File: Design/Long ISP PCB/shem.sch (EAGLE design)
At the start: 49 parts, among them IC1 4511N, IC2 4511N, J1 9V_POWER_JACK, Q1 600mA/40V, Q2 600mA/40V, Q3 600mA/40V, Q4 600mA/40V, Q5 600mA/40V, U2 328P, U3 SN74HC595N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

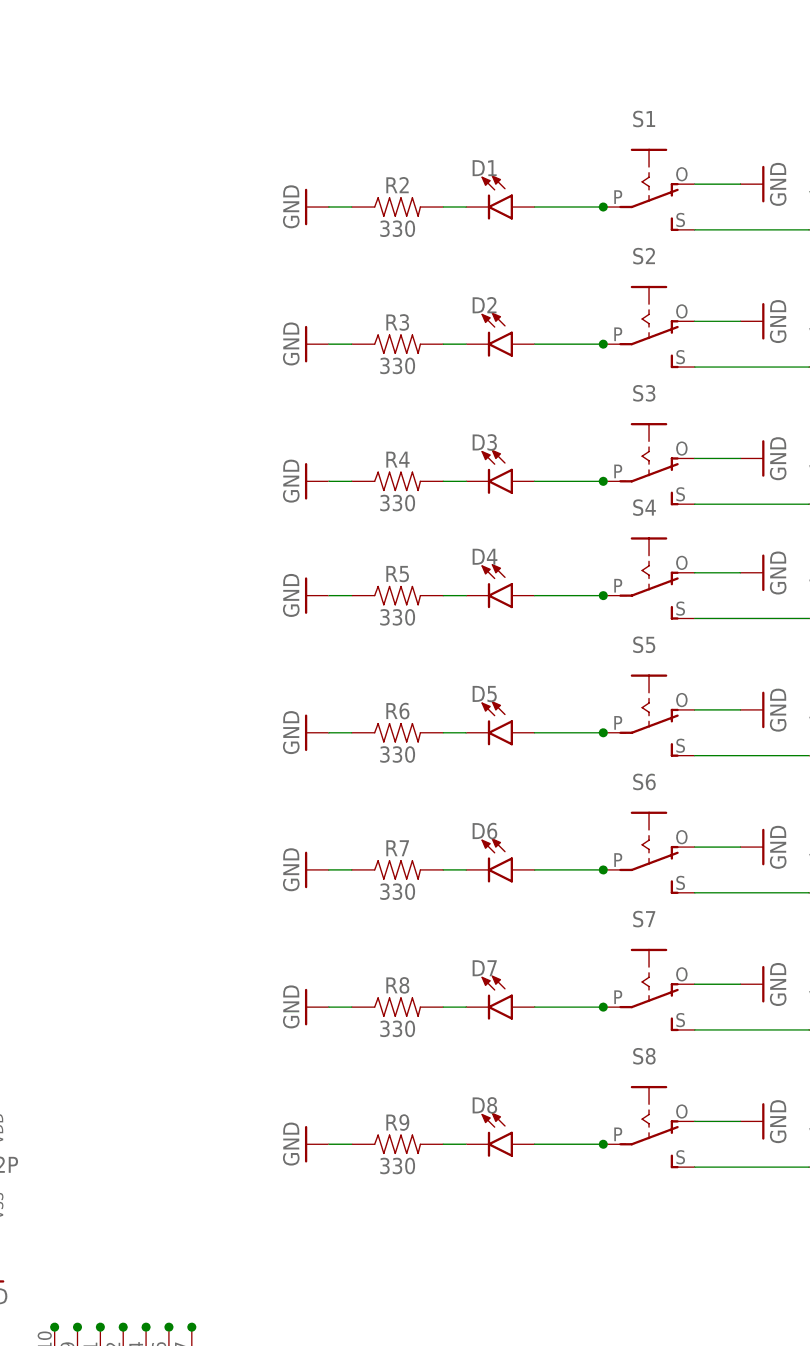
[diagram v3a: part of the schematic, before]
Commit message: fixed board schematic consistency sync issue as a result leds for input switches have been removed again
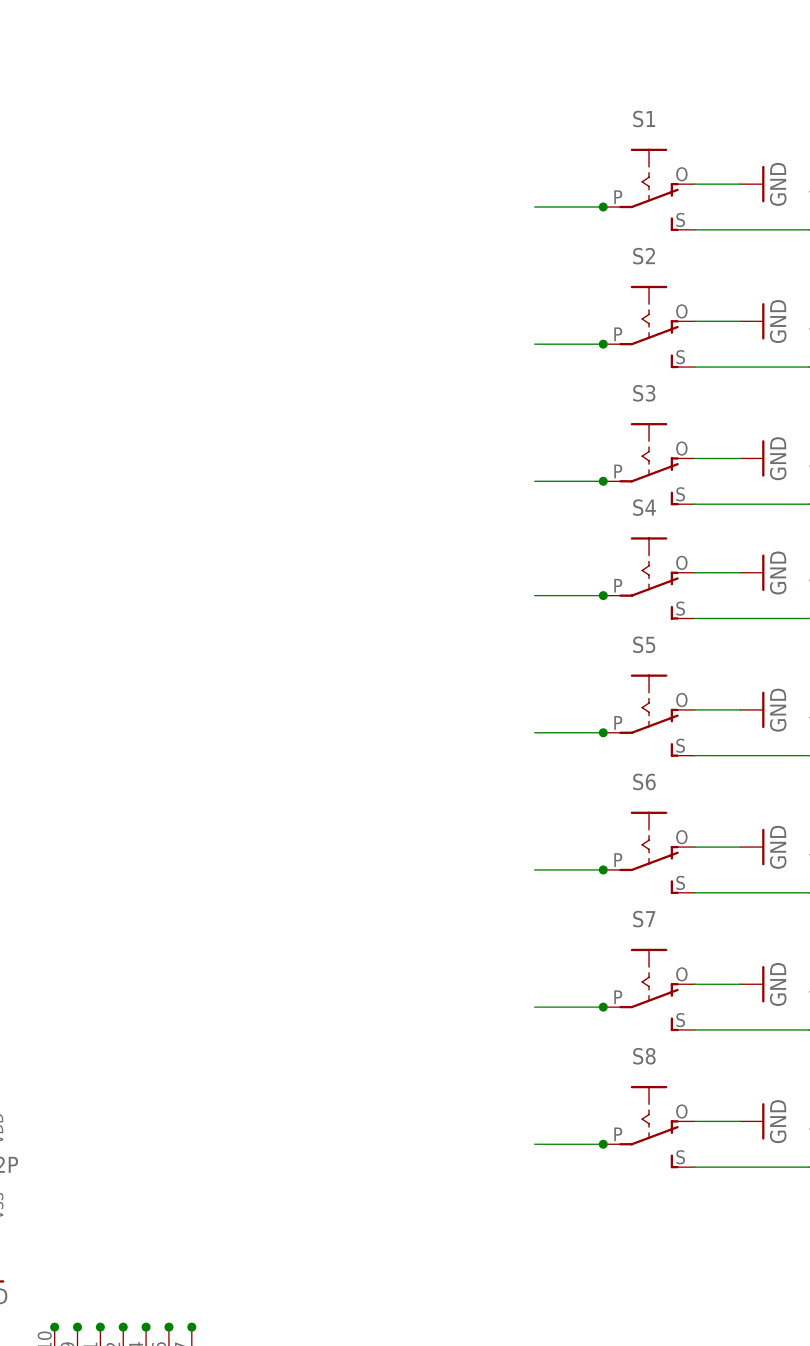
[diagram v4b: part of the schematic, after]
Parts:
- removed D1, D2, D3, D4, D5, D6, D7, D8: (no value), SparkFun-LED:LED3MM
- removed R2, R3, R4, R5, R6, R7, R8, R9: 330, SparkFun-Resistors:330OHM-HORIZ-1/10W-5%
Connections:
- removed net N$12: D1.C, R2.2
- removed net N$13: D2.C, R3.2
- removed net N$14: D3.C, R4.2
- removed net N$15: D5.C, R6.2
- removed net N$17: D6.C, R7.2
- removed net N$18: D7.C, R8.2
- removed net N$19: D8.C, R9.2
- removed net N$20: D4.C, R5.2
- net GND: no longer R2.1, R3.1, R4.1, R5.1, R6.1, R7.1, R8.1, R9.1
- net S0: no longer D1.A
- net S1: no longer D2.A
- net S2: no longer D3.A
- net S3: no longer D4.A
- net S4: no longer D5.A
- net S5: no longer D6.A
- net S6: no longer D7.A
- net S7: no longer D8.A
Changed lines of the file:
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@@
 <part name="GND23" library="supply1" deviceset="GND" device=""/>
 <part name="GND24" library="supply1" deviceset="GND" device=""/>
-<part name="D1" library="SparkFun-LED" deviceset="LED" device="3MM"/>
-<part name="D2" library="SparkFun-LED" deviceset="LED" device="3MM"/>
-<part name="D3" library="SparkFun-LED" deviceset="LED" device="3MM"/>
-<part name="D4" library="SparkFun-LED" deviceset="LED" device="3MM"/>
-<part name="D5" library="SparkFun-LED" deviceset="LED" device="3MM"/>
-<part name="D6" library="SparkFun-LED" deviceset="LED" device="3MM"/>
-<part name="D7" library="SparkFun-LED" deviceset="LED" device="3MM"/>
-<part name="D8" library="SparkFun-LED" deviceset="LED" device="3MM"/>
 <part name="P+5" library="supply1" deviceset="VCC" device=""/>
 <part name="P+7" library="supply1" deviceset="VCC" device=""/>
@@
 <part name="PWR" library="adafruit" deviceset="EG1218" device="S"/>
 <part name="P+1" library="supply1" deviceset="VCC" device=""/>
-<part name="R2" library="SparkFun-Resistors" deviceset="330OHM" device="-HORIZ-1/10W-5%" value="330"/>
-<part name="R3" library="SparkFun-Resistors" deviceset="330OHM" device="-HORIZ-1/10W-5%" value="330"/>
-<part name="R4" library="SparkFun-Resistors" deviceset="330OHM" device="-HORIZ-1/10W-5%" value="330"/>
-<part name="R5" library="SparkFun-Resistors" deviceset="330OHM" device="-HORIZ-1/10W-5%" value="330"/>
-<part name="R6" library="SparkFun-Resistors" deviceset="330OHM" device="-HORIZ-1/10W-5%" value="330"/>
-<part name="R7" library="SparkFun-Resistors" deviceset="330OHM" device="-HORIZ-1/10W-5%" value="330"/>
-<part name="R8" library="SparkFun-Resistors" deviceset="330OHM" device="-HORIZ-1/10W-5%" value="330"/>
-<part name="R9" library="SparkFun-Resistors" deviceset="330OHM" device="-HORIZ-1/10W-5%" value="330"/>
-<part name="GND25" library="supply1" deviceset="GND" device=""/>
-<part name="GND26" library="supply1" deviceset="GND" device=""/>
-<part name="GND27" library="supply1" deviceset="GND" device=""/>
-<part name="GND28" library="supply1" deviceset="GND" device=""/>
-<part name="GND29" library="supply1" deviceset="GND" device=""/>
-<part name="GND30" library="supply1" deviceset="GND" device=""/>
-<part name="GND31" library="supply1" deviceset="GND" device=""/>
-<part name="GND32" library="supply1" deviceset="GND" device=""/>
 </parts>
 <sheets>
@@
 <instance part="IC2" gate="P" x="137.16" y="43.18"/>
 <instance part="GND24" gate="1" x="137.16" y="30.48"/>
-<instance part="D1" gate="G$1" x="195.58" y="149.86" rot="R270"/>
-<instance part="D2" gate="G$1" x="195.58" y="134.62" rot="R270"/>
-<instance part="D3" gate="G$1" x="195.58" y="119.38" rot="R270"/>
-<instance part="D4" gate="G$1" x="195.58" y="106.68" rot="R270"/>
-<instance part="D5" gate="G$1" x="195.58" y="91.44" rot="R270"/>
-<instance part="D6" gate="G$1" x="195.58" y="76.2" rot="R270"/>
-<instance part="D7" gate="G$1" x="195.58" y="60.96" rot="R270"/>
-<instance part="D8" gate="G$1" x="195.58" y="45.72" rot="R270"/>
 <instance part="P+5" gate="VCC" x="-33.02" y="58.42"/>
 <instance part="P+7" gate="VCC" x="-17.78" y="60.96"/>
@@
 <instance part="PWR" gate="1" x="33.02" y="114.3" rot="R180"/>
 <instance part="P+1" gate="VCC" x="30.48" y="124.46"/>
-<instance part="R2" gate="G$1" x="182.88" y="149.86"/>
-<instance part="R3" gate="G$1" x="182.88" y="134.62"/>
-<instance part="R4" gate="G$1" x="182.88" y="119.38"/>
-<instance part="R5" gate="G$1" x="182.88" y="106.68"/>
-<instance part="R6" gate="G$1" x="182.88" y="91.44"/>
-<instance part="R7" gate="G$1" x="182.88" y="76.2"/>
-<instance part="R8" gate="G$1" x="182.88" y="60.96"/>
-<instance part="R9" gate="G$1" x="182.88" y="45.72"/>
-<instance part="GND25" gate="1" x="172.72" y="45.72" rot="R270"/>
-<instance part="GND26" gate="1" x="172.72" y="60.96" rot="R270"/>
-<instance part="GND27" gate="1" x="172.72" y="76.2" rot="R270"/>
-<instance part="GND28" gate="1" x="172.72" y="91.44" rot="R270"/>
-<instance part="GND29" gate="1" x="172.72" y="106.68" rot="R270"/>
-<instance part="GND30" gate="1" x="172.72" y="119.38" rot="R270"/>
-<instance part="GND31" gate="1" x="172.72" y="134.62" rot="R270"/>
-<instance part="GND32" gate="1" x="172.72" y="149.86" rot="R270"/>
 </instances>
 <busses>
@@
 <wire x1="50.8" y1="-20.32" x2="50.8" y2="-17.78" width="0.1524" layer="91"/>
 </segment>
-<segment>
-<pinref part="R9" gate="G$1" pin="1"/>
-<pinref part="GND25" gate="1" pin="GND"/>
-<wire x1="175.26" y1="45.72" x2="177.8" y2="45.72" width="0.1524" layer="91"/>
-</segment>
-<segment>
-<pinref part="R8" gate="G$1" pin="1"/>
-<pinref part="GND26" gate="1" pin="GND"/>
-<wire x1="175.26" y1="60.96" x2="177.8" y2="60.96" width="0.1524" layer="91"/>
-</segment>
-<segment>
-<pinref part="R7" gate="G$1" pin="1"/>
-<pinref part="GND27" gate="1" pin="GND"/>
-<wire x1="175.26" y1="76.2" x2="177.8" y2="76.2" width="0.1524" layer="91"/>
-</segment>
-<segment>
-<pinref part="R6" gate="G$1" pin="1"/>
-<pinref part="GND28" gate="1" pin="GND"/>
-<wire x1="175.26" y1="91.44" x2="177.8" y2="91.44" width="0.1524" layer="91"/>
-</segment>
-<segment>
-<pinref part="R5" gate="G$1" pin="1"/>
-<pinref part="GND29" gate="1" pin="GND"/>
-<wire x1="175.26" y1="106.68" x2="177.8" y2="106.68" width="0.1524" layer="91"/>
-</segment>
-<segment>
-<pinref part="R4" gate="G$1" pin="1"/>
-<pinref part="GND30" gate="1" pin="GND"/>
-<wire x1="175.26" y1="119.38" x2="177.8" y2="119.38" width="0.1524" layer="91"/>
-</segment>
-<segment>
-<pinref part="R3" gate="G$1" pin="1"/>
-<pinref part="GND31" gate="1" pin="GND"/>
-<wire x1="175.26" y1="134.62" x2="177.8" y2="134.62" width="0.1524" layer="91"/>
-</segment>
-<segment>
-<pinref part="R2" gate="G$1" pin="1"/>
-<pinref part="GND32" gate="1" pin="GND"/>
-<wire x1="175.26" y1="149.86" x2="177.8" y2="149.86" width="0.1524" layer="91"/>
-</segment>
 </net>
 <net name="SCK" class="0">
@@
 <pinref part="S1" gate="1" pin="P"/>
 <junction x="205.74" y="149.86"/>
-<pinref part="D1" gate="G$1" pin="A"/>
 <wire x1="198.12" y1="149.86" x2="205.74" y2="149.86" width="0.1524" layer="91"/>
 </segment>
@@
 <pinref part="S2" gate="1" pin="P"/>
 <junction x="205.74" y="134.62"/>
-<pinref part="D2" gate="G$1" pin="A"/>
 <wire x1="198.12" y1="134.62" x2="205.74" y2="134.62" width="0.1524" layer="91"/>
 </segment>
@@
 <pinref part="S3" gate="1" pin="P"/>
 <junction x="205.74" y="119.38"/>
-<pinref part="D3" gate="G$1" pin="A"/>
 <wire x1="198.12" y1="119.38" x2="205.74" y2="119.38" width="0.1524" layer="91"/>
 </segment>
@@
 <pinref part="S4" gate="1" pin="P"/>
 <junction x="205.74" y="106.68"/>
-<pinref part="D4" gate="G$1" pin="A"/>
 <wire x1="198.12" y1="106.68" x2="205.74" y2="106.68" width="0.1524" layer="91"/>
 </segment>
@@
 <pinref part="S5" gate="1" pin="P"/>
 <junction x="205.74" y="91.44"/>
-<pinref part="D5" gate="G$1" pin="A"/>
 <wire x1="198.12" y1="91.44" x2="205.74" y2="91.44" width="0.1524" layer="91"/>
 </segment>
@@
 <pinref part="S7" gate="1" pin="P"/>
 <junction x="205.74" y="60.96"/>
-<pinref part="D7" gate="G$1" pin="A"/>
 <wire x1="198.12" y1="60.96" x2="205.74" y2="60.96" width="0.1524" layer="91"/>
 </segment>
@@
 <pinref part="S6" gate="1" pin="P"/>
 <junction x="205.74" y="76.2"/>
-<pinref part="D6" gate="G$1" pin="A"/>
 <wire x1="198.12" y1="76.2" x2="205.74" y2="76.2" width="0.1524" layer="91"/>
 </segment>
@@
 <pinref part="S8" gate="1" pin="P"/>
 <junction x="205.74" y="45.72"/>
-<pinref part="D8" gate="G$1" pin="A"/>
 <wire x1="198.12" y1="45.72" x2="205.74" y2="45.72" width="0.1524" layer="91"/>
 </segment>
@@
 </segment>
 </net>
-<net name="N$12" class="0">
-<segment>
-<pinref part="D1" gate="G$1" pin="C"/>
-<pinref part="R2" gate="G$1" pin="2"/>
-<wire x1="187.96" y1="149.86" x2="190.5" y2="149.86" width="0.1524" layer="91"/>
-</segment>
-</net>
-<net name="N$13" class="0">
-<segment>
-<pinref part="D2" gate="G$1" pin="C"/>
-<pinref part="R3" gate="G$1" pin="2"/>
-<wire x1="187.96" y1="134.62" x2="190.5" y2="134.62" width="0.1524" layer="91"/>
-</segment>
-</net>
-<net name="N$14" class="0">
-<segment>
-<pinref part="D3" gate="G$1" pin="C"/>
-<pinref part="R4" gate="G$1" pin="2"/>
-<wire x1="187.96" y1="119.38" x2="190.5" y2="119.38" width="0.1524" layer="91"/>
-</segment>
-</net>
-<net name="N$15" class="0">
-<segment>
-<pinref part="D5" gate="G$1" pin="C"/>
-<pinref part="R6" gate="G$1" pin="2"/>
-<wire x1="187.96" y1="91.44" x2="190.5" y2="91.44" width="0.1524" layer="91"/>
-</segment>
-</net>
-<net name="N$17" class="0">
-<segment>
-<pinref part="D6" gate="G$1" pin="C"/>
-<pinref part="R7" gate="G$1" pin="2"/>
-<wire x1="187.96" y1="76.2" x2="190.5" y2="76.2" width="0.1524" layer="91"/>
-</segment>
-</net>
-<net name="N$18" class="0">
-<segment>
-<pinref part="D7" gate="G$1" pin="C"/>
-<pinref part="R8" gate="G$1" pin="2"/>
-<wire x1="187.96" y1="60.96" x2="190.5" y2="60.96" width="0.1524" layer="91"/>
-</segment>
-</net>
-<net name="N$19" class="0">
-<segment>
-<pinref part="D8" gate="G$1" pin="C"/>
-<pinref part="R9" gate="G$1" pin="2"/>
-<wire x1="187.96" y1="45.72" x2="190.5" y2="45.72" width="0.1524" layer="91"/>
-</segment>
-</net>
-<net name="N$20" class="0">
-<segment>
-<pinref part="D4" gate="G$1" pin="C"/>
-<pinref part="R5" gate="G$1" pin="2"/>
-<wire x1="187.96" y1="106.68" x2="190.5" y2="106.68" width="0.1524" layer="91"/>
-</segment>
-</net>
